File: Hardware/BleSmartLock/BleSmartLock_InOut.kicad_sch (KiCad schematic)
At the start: 66 parts, among them J10 Conn_01x04, J11 Conn_01x04, J12 Conn_01x02, J8 Conn_01x03, J9 Conn_01x04, Q10 NX7002AKA, Q11 PMV50UPE, Q12 NX7002AKA, Q13 NX7002AKA, Q14 NX7002AKA, Q3 NX7002AKA, Q4 PMV50UPE, Q5 NX7002AKA, Q6 NX7002AKA, Q7 PMV50UPE, Q8 NX7002AKA, Q9 PMV50UPE, U4 LMV611

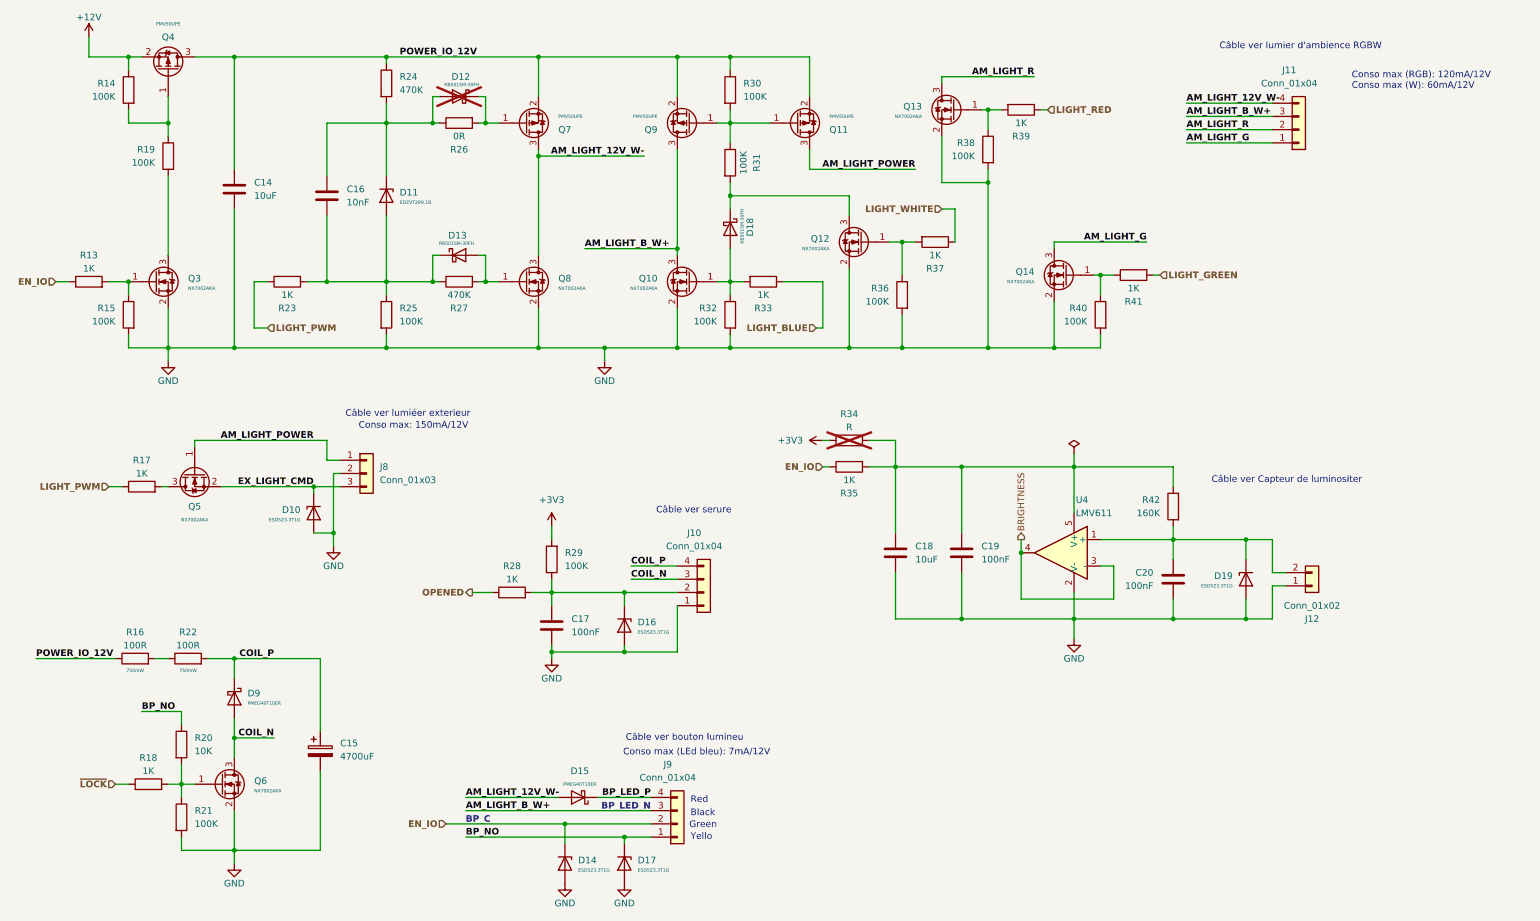
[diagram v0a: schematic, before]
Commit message: Ajout carte BleSmartLock
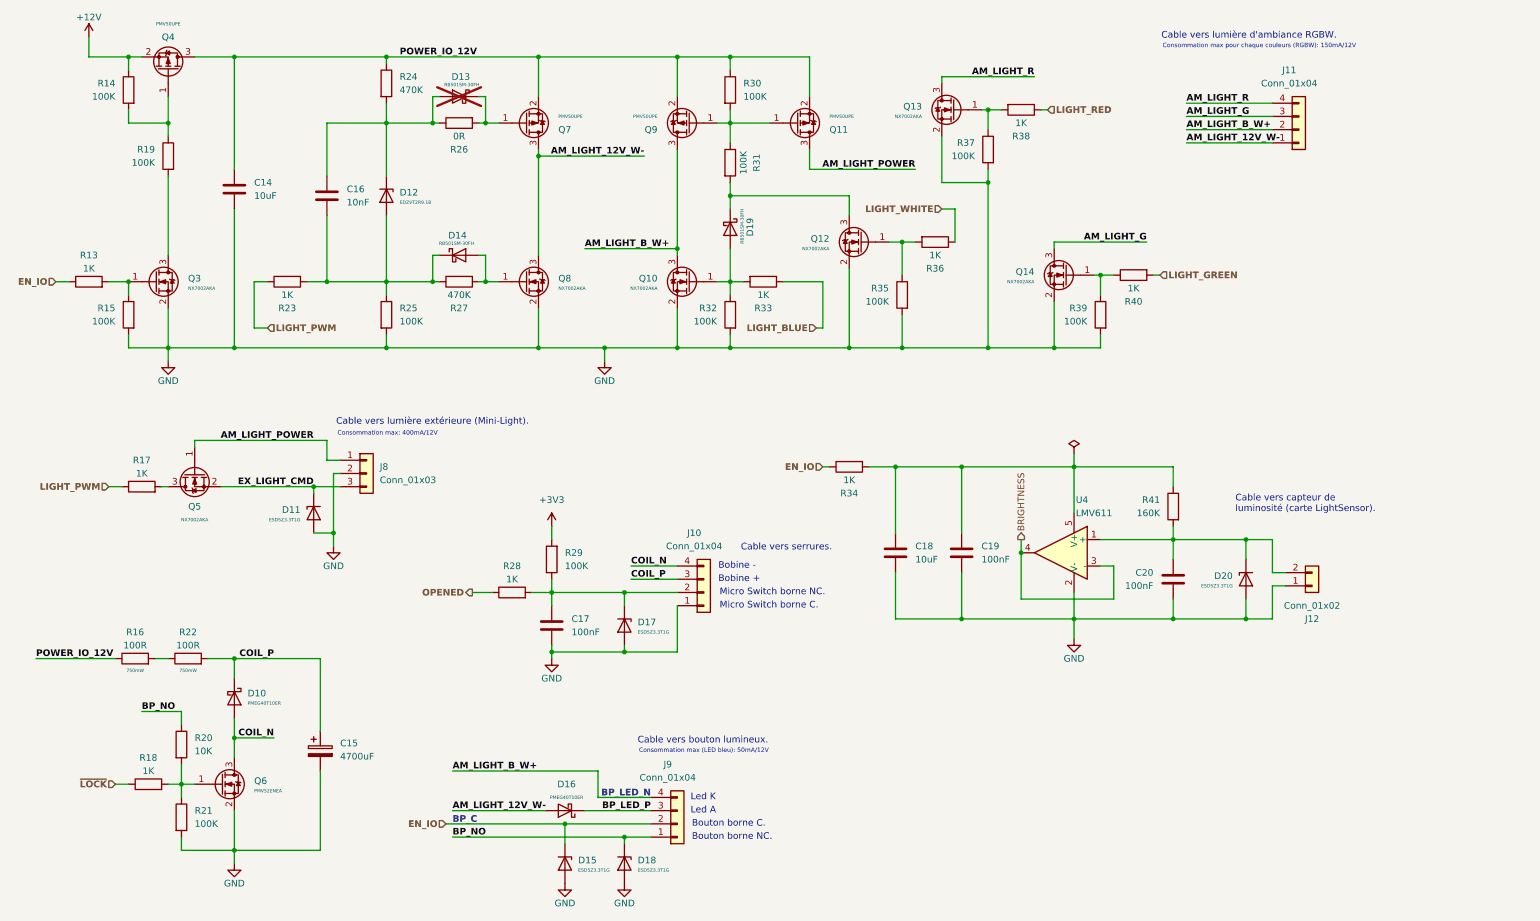
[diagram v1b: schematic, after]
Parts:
- removed R34: R, Resistor_SMD:R_0402_1005Metric_Pad0.72x0.64mm_HandSolder, symbol Device:R
- C15: footprint Capacitor_THT:CP_Radial_D16.0mm_P7.50mm -> AM163:CP_Radial_L25.0mm_D16.0mm_P7.50mm_Horizontal_EdgeCuts
- Q6: value NX7002AKA -> PMV52ENEA; Vendor Nexperia:NX7002AKA -> Nexperia:PMV52ENEA
- U4: footprint Package_TO_SOT_SMD:SOT-353_SC-70-5 -> Package_TO_SOT_SMD:SOT-23-5
- renumbered D9 to D10, D10 to D11, D11 to D12, D12 to D13, D13 to D14, D14 to D15, D15 to D16, D16 to D17, D17 to D18, D18 to D19, D19 to D20, R35 to R34, R36 to R35, R37 to R36, R38 to R37, R39 to R38, R40 to R39, R41 to R40, R42 to R41
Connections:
- net AM_LIGHT_12V_W-: now also J11.1 (Pin_1); no longer J11.4 (Pin_4)
- net AM_LIGHT_B_W+: now also J11.2 (Pin_2), J9.4 (Pin_4); no longer J11.3 (Pin_3), J9.3 (Pin_3)
- net AM_LIGHT_G: now also J11.3 (Pin_3); no longer J11.1 (Pin_1)
- net AM_LIGHT_R: now also J11.4 (Pin_4); no longer J11.2 (Pin_2)
- net BP_LED_P: now also J9.3 (Pin_3); no longer J9.4 (Pin_4)
- net COIL_N: now also J10.4 (Pin_4); no longer J10.3 (Pin_3)
- net COIL_P: now also J10.3 (Pin_3); no longer J10.4 (Pin_4)
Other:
- note added: "Bobine +"
- note added: "Bobine -"
- note added: "Bouton borne C."
- note added: "Bouton borne NC."
- note added: "Cable vers bouton lumineux."
- note added: "Cable vers capteur de luminosité (carte LightSensor)."
- note added: "Cable vers lumière d'ambiance RGBW."
- note added: "Cable vers lumière extérieure (Mini-Light)."
- note added: "Cable vers serrures."
- note added: "Consommation max (LED bleu): 50mA/12V"
- note added: "Consommation max pour chaque couleurs (RGBW): 150mA/12V"
- note added: "Consommation max: 400mA/12V"
- note added: "Led A"
- note added: "Led K"
- note added: "Micro Switch borne C."
- note added: "Micro Switch borne NC."
- note removed: "Black"
- note removed: "Conso max (LEd bleu): 7mA/12V"
- note removed: "Conso max (RGB): 120mA/12V Conso max (W): 60mA/12V"
- note removed: "Conso max: 150mA/12V"
- note removed: "Câble ver Capteur de luminositer"
- note removed: "Câble ver bouton lumineu"
- note removed: "Câble ver lumier d'ambience RGBW"
- note removed: "Câble ver lumiéer exterieur"
- note removed: "Câble ver serure"
- note removed: "Green"
- note removed: "Red"
- note removed: "Yello"
- company: (none) -> antoine163
- title: (none) -> Ble Smart Lock
- moved on the sheet: D16

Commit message: Mise a jour pcb en v1.1 et readme
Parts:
- C15: Vendor (none) -> PANASONIC:ECA1CAM472X
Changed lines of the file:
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@@
 	(title_block
 		(title "Ble Smart Lock")
-		(date "2024-03-30")
-		(rev "v1.0")
+		(date "2024-05-18")
+		(rev "v1.1")
 		(company "antoine163")
 	)
@@
 			(at 76.2 160.02 0)
 			(effects
+				(font
+					(size 1.27 1.27)
+				)
+				(hide yes)
+			)
+		)
+		(property "Vendor" "     PANASONIC:ECA1CAM472X"
+			(at 76.2 160.02 0)
+			(effects
